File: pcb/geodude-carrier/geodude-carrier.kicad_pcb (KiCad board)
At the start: 2 copper layers, 112.5 x 135.2 mm, 48 parts, among them J1 12V, J2 12V, J3 GND, J30 SCL, J31 SCL, J32 SDA, J33 SDA, J34 3V3, J35 3V3, J36 5V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

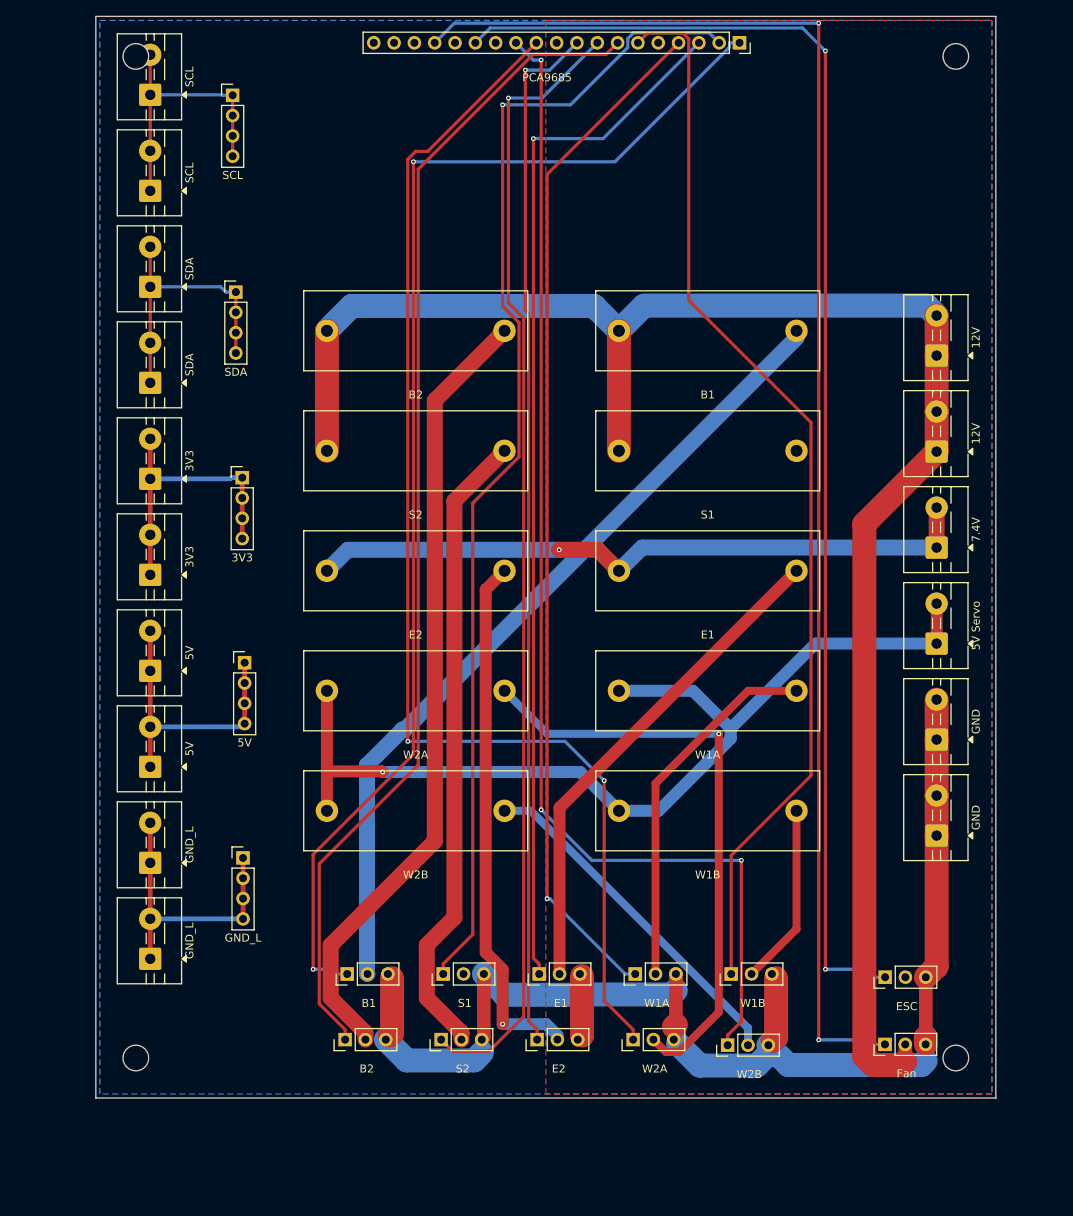
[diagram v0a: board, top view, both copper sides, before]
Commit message: Aligned left terminals and servo rows, unrouted - needs placement review
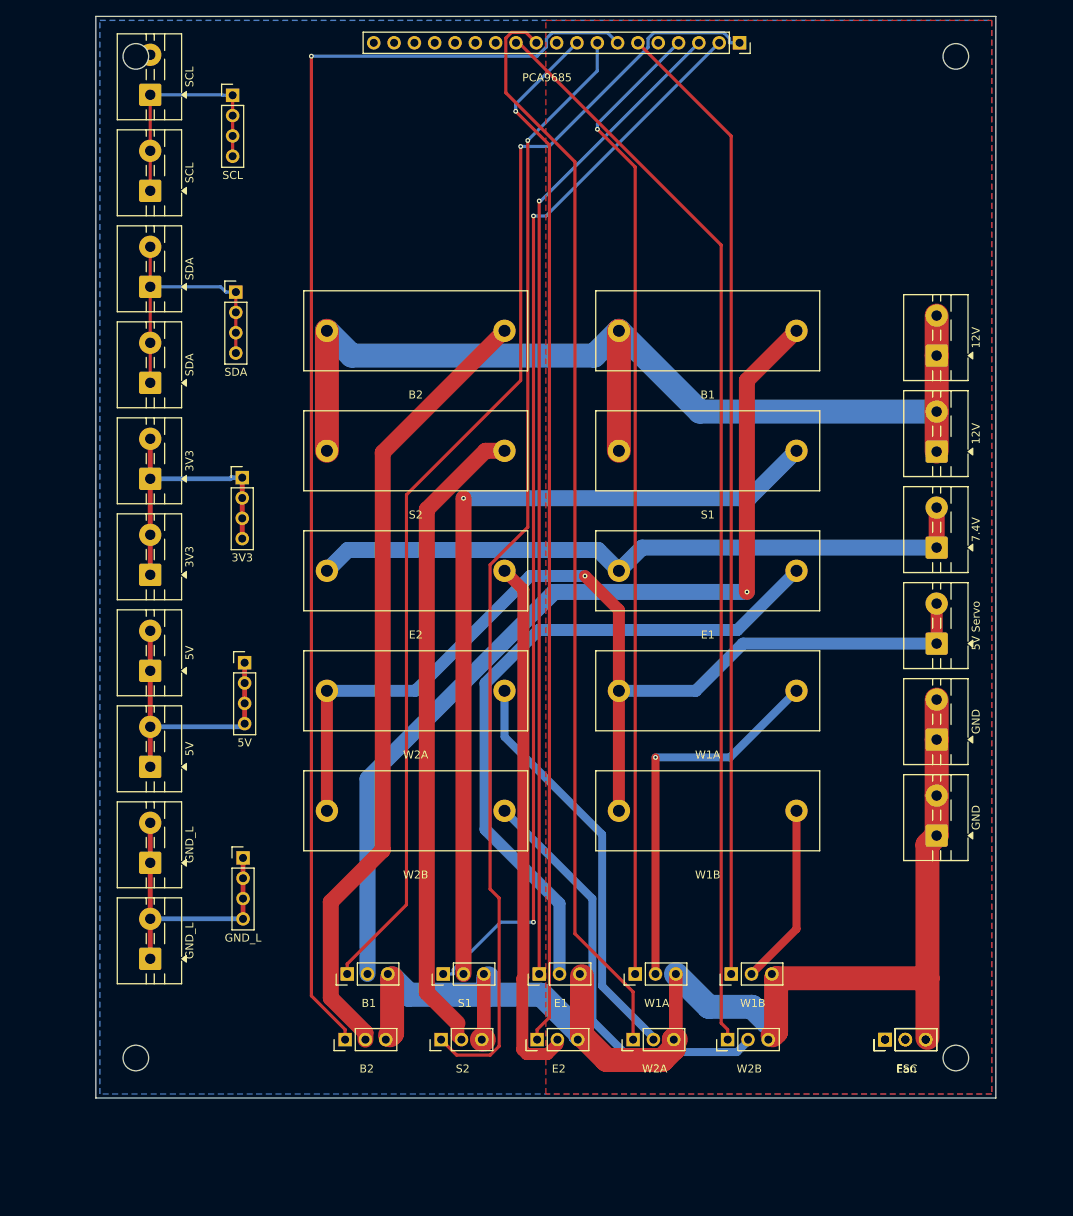
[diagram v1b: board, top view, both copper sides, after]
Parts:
- moved J_ESC 7.80 mm to (116.5, 132.5)
- moved SV10 0.70 mm to (96.8, 132.5)
- moved J_FAN 0.60 mm to (116.4, 132.5)
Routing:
- net PWM_CH12: track 184.6 -> 0.00 mm, vias 2 -> 0
- net PWM_CH11: track 168.4 -> 0.00 mm, vias 2 -> 0
- net SV2_PWR: track 0.00 -> 103.6 mm, vias 0 -> 1
- net +12V: track 214.8 -> 130.0 mm
- net SV9_PWR: track 74.7 -> 51.3 mm, vias 1 -> 0
- net SV3_PWR: track 62.7 -> 84.9 mm
- net PWM_CH8: track 155.3 -> 136.4 mm, vias 2 -> 0
- net PWM_CH5: track 146.7 -> 165.3 mm, vias 0 -> 1
- net SV1_PWR: track 102.8 -> 116.7 mm, vias 0 -> 1
- net PWM_CH9: track 149.2 -> 135.8 mm, vias 3 -> 0
- net PWM_CH4: track 134.6 -> 121.2 mm
- net PWM_CH0: track 157.9 -> 147.2 mm, vias 2 -> 1
- net PWM_CH1: track 145.4 -> 134.7 mm, vias 1 -> 2
- net SV10_PWR: track 43.8 -> 52.6 mm
- net +5V_SERVO: track 123.6 -> 131.5 mm
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
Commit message: Remove duplicate left screw terminals - 1x per bus now
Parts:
- removed J30: SCL, TerminalBlock_MaiXu_MX126-5.0-02P_1x02_P5.00mm
- removed J33: SDA, TerminalBlock_MaiXu_MX126-5.0-02P_1x02_P5.00mm
- removed J35: 3V3, TerminalBlock_MaiXu_MX126-5.0-02P_1x02_P5.00mm
- removed J36: 5V, TerminalBlock_MaiXu_MX126-5.0-02P_1x02_P5.00mm
- removed J38: GND_L, TerminalBlock_MaiXu_MX126-5.0-02P_1x02_P5.00mm

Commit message: Left bus: screw+header pairs aligned, 12mm spacing
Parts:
- moved J44 35.3 mm to (24.0, 76.7)
- moved J39 34.8 mm to (12.0, 78.0)
- moved J43 24.1 mm to (24.0, 64.7)
- moved J37 24.0 mm to (12.0, 66.0)
- moved J31 20.1 mm to (12.0, 30.0)
- moved J40 17.9 mm to (24.0, 28.7)
- moved J42 15.4 mm to (24.0, 52.7)
- moved J34 15.1 mm to (12.0, 54.0)
- moved J32 13.1 mm to (12.0, 42.0)
- moved J41 11.4 mm to (24.0, 40.7)
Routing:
- net GND_LOGIC: track 36.2 -> 53.2 mm
- net +5V_LOGIC: track 36.6 -> 19.6 mm
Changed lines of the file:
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@@
 	(footprint "PinHeader_1x04_P2.54mm_Vertical"
 		(layer "F.Cu")
-		(at 35.3 39.06)
+		(at 24 40.7)
 		(descr "Through hole straight pin header, 1x04, 2.54mm pitch, single row")
 		(tags "Through hole pin header THT 1x04 2.54mm single row")
@@
 	(footprint "TerminalBlock_MaiXu_MX126-5.0-02P_1x02_P5.00mm"
 		(layer "F.Cu")
-		(at 24.6 62.4 90)
+		(at 12 54 90)
 		(descr "terminal block MaiXu MX126-5.0-02P, 2 pins, pitch 5mm, size 10.5x7.8mm, drill diameter 1.3mm, pad diameter 2.8mm, https://www.lcsc.com/datasheet/lcsc_datasheet_2309150913_MAX-MX126-5-0-03P-GN01-Cu-S-A_C5188435.pdf")
 		(tags "THT terminal block MaiXu MX126-5.0-02P pitch 5mm size 10.5x7.8mm drill 1.3mm pad 2.8mm")
@@
 	(footprint "TerminalBlock_MaiXu_MX126-5.0-02P_1x02_P5.00mm"
 		(layer "F.Cu")
-		(at 24.6 38.4 90)
+		(at 12 42 90)
 		(descr "terminal block MaiXu MX126-5.0-02P, 2 pins, pitch 5mm, size 10.5x7.8mm, drill diameter 1.3mm, pad diameter 2.8mm, https://www.lcsc.com/datasheet/lcsc_datasheet_2309150913_MAX-MX126-5-0-03P-GN01-Cu-S-A_C5188435.pdf")
 		(tags "THT terminal block MaiXu MX126-5.0-02P pitch 5mm size 10.5x7.8mm drill 1.3mm pad 2.8mm")
@@
 	(footprint "TerminalBlock_MaiXu_MX126-5.0-02P_1x02_P5.00mm"
 		(layer "F.Cu")
-		(at 24.6 86.4 90)
+		(at 12 66 90)
 		(descr "terminal block MaiXu MX126-5.0-02P, 2 pins, pitch 5mm, size 10.5x7.8mm, drill diameter 1.3mm, pad diameter 2.8mm, https://www.lcsc.com/datasheet/lcsc_datasheet_2309150913_MAX-MX126-5-0-03P-GN01-Cu-S-A_C5188435.pdf")
 		(tags "THT terminal block MaiXu MX126-5.0-02P pitch 5mm size 10.5x7.8mm drill 1.3mm pad 2.8mm")
@@
 	(footprint "PinHeader_1x04_P2.54mm_Vertical"
 		(layer "F.Cu")
-		(at 36.2 109.79)
+		(at 24 76.7)
 		(descr "Through hole straight pin header, 1x04, 2.54mm pitch, single row")
 		(tags "Through hole pin header THT 1x04 2.54mm single row")
@@
 	(footprint "PinHeader_1x04_P2.54mm_Vertical"
 		(layer "F.Cu")
-		(at 36.4 85.39)
+		(at 24 64.7)
 		(descr "Through hole straight pin header, 1x04, 2.54mm pitch, single row")
 		(tags "Through hole pin header THT 1x04 2.54mm single row")
@@
 	(footprint "TerminalBlock_MaiXu_MX126-5.0-02P_1x02_P5.00mm"
 		(layer "F.Cu")
-		(at 24.6 110.4 90)
+		(at 12 78 90)
 		(descr "terminal block MaiXu MX126-5.0-02P, 2 pins, pitch 5mm, size 10.5x7.8mm, drill diameter 1.3mm, pad diameter 2.8mm, https://www.lcsc.com/datasheet/lcsc_datasheet_2309150913_MAX-MX126-5-0-03P-GN01-Cu-S-A_C5188435.pdf")
 		(tags "THT terminal block MaiXu MX126-5.0-02P pitch 5mm size 10.5x7.8mm drill 1.3mm pad 2.8mm")
@@
 	(footprint "PinHeader_1x04_P2.54mm_Vertical"
 		(layer "F.Cu")
-		(at 34.9 14.46)
+		(at 24 28.7)
 		(descr "Through hole straight pin header, 1x04, 2.54mm pitch, single row")
 		(tags "Through hole pin header THT 1x04 2.54mm single row")
@@
 	(footprint "TerminalBlock_MaiXu_MX126-5.0-02P_1x02_P5.00mm"
 		(layer "F.Cu")
-		(at 24.6 14.4 90)
+		(at 12 30 90)
 		(descr "terminal block MaiXu MX126-5.0-02P, 2 pins, pitch 5mm, size 10.5x7.8mm, drill diameter 1.3mm, pad diameter 2.8mm, https://www.lcsc.com/datasheet/lcsc_datasheet_2309150913_MAX-MX126-5-0-03P-GN01-Cu-S-A_C5188435.pdf")
 		(tags "THT terminal block MaiXu MX126-5.0-02P pitch 5mm size 10.5x7.8mm drill 1.3mm pad 2.8mm")
@@
 	(footprint "PinHeader_1x04_P2.54mm_Vertical"
 		(layer "F.Cu")
-		(at 36.1 62.26)
+		(at 24 52.7)
 		(descr "Through hole straight pin header, 1x04, 2.54mm pitch, single row")
 		(tags "Through hole pin header THT 1x04 2.54mm single row")
@@
 	)
 	(segment
-		(start 24.6 93.4)
-		(end 24.6 86.4)
-		(width 0.6)
-		(layer "F.Cu")
-		(net "+5V_LOGIC")
-	)
-	(segment
-		(start 24.6 81.4)
-		(end 24.6 86.4)
-		(width 0.6)
-		(layer "F.Cu")
-		(net "+5V_LOGIC")
-	)
-	(segment
-		(start 24.6 98.4)
-		(end 24.6 93.4)
-		(width 0.6)
-		(layer "F.Cu")
-		(net "+5V_LOGIC")
-	)
-	(segment
 		(start 36.4 93.01)
 		(end 36.4 90.47)
@@
 	)
 	(segment
+		(start 24.6 93.4)
+		(end 24.6 86.4)
+		(width 0.6)
+		(layer "F.Cu")
+		(net "GND_LOGIC")
+	)
+	(segment
 		(start 24.6 117.4)
 		(end 24.6 110.4)
@@
 		(width 0.6)
 		(layer "F.Cu")
+		(net "GND_LOGIC")
+	)
+	(segment
+		(start 24.6 81.4)
+		(end 24.6 86.4)
+		(width 0.6)
+		(layer "F.Cu")
+		(net "GND_LOGIC")
+	)
+	(segment
+		(start 24.6 98.4)
+		(end 24.6 93.4)
+		(width 0.6)
+		(layer "F.Cu")

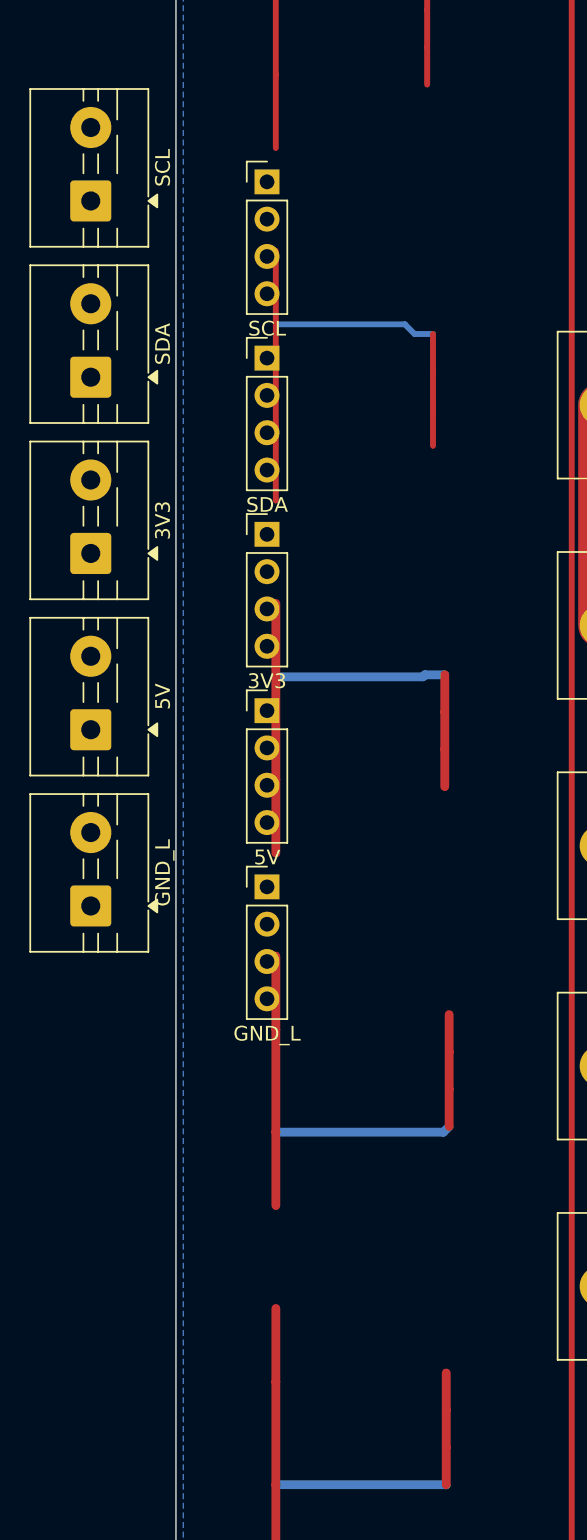
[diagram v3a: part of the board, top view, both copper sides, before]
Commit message: Spacing update
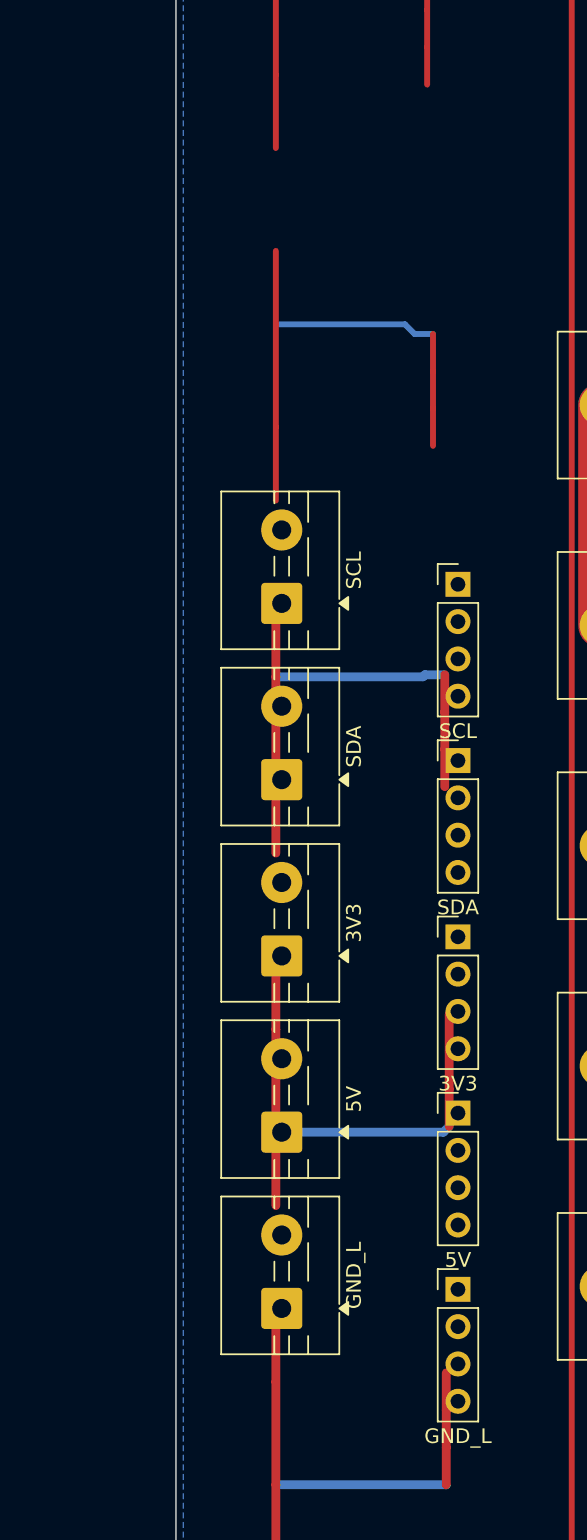
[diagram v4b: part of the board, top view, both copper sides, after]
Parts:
- moved J40 30.3 mm to (37.0, 56.1)
- moved J31 30.3 mm to (25.0, 57.4)
- moved J32 30.3 mm to (25.0, 69.4)
- moved J34 30.3 mm to (25.0, 81.4)
- moved J37 30.3 mm to (25.0, 93.4)
- moved J39 30.3 mm to (25.0, 105.4)
- moved J41 30.3 mm to (37.0, 68.1)
- moved J42 30.3 mm to (37.0, 80.1)
- moved J43 30.3 mm to (37.0, 92.1)
- moved J44 30.3 mm to (37.0, 104.1)
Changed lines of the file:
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@@
 	(footprint "PinHeader_1x04_P2.54mm_Vertical"
 		(layer "F.Cu")
-		(at 24 40.7)
+		(at 37 68.1)
 		(descr "Through hole straight pin header, 1x04, 2.54mm pitch, single row")
 		(tags "Through hole pin header THT 1x04 2.54mm single row")
@@
 	(footprint "TerminalBlock_MaiXu_MX126-5.0-02P_1x02_P5.00mm"
 		(layer "F.Cu")
-		(at 12 54 90)
+		(at 25 81.4 90)
 		(descr "terminal block MaiXu MX126-5.0-02P, 2 pins, pitch 5mm, size 10.5x7.8mm, drill diameter 1.3mm, pad diameter 2.8mm, https://www.lcsc.com/datasheet/lcsc_datasheet_2309150913_MAX-MX126-5-0-03P-GN01-Cu-S-A_C5188435.pdf")
 		(tags "THT terminal block MaiXu MX126-5.0-02P pitch 5mm size 10.5x7.8mm drill 1.3mm pad 2.8mm")
@@
 	(footprint "TerminalBlock_MaiXu_MX126-5.0-02P_1x02_P5.00mm"
 		(layer "F.Cu")
-		(at 12 42 90)
+		(at 25 69.4 90)
 		(descr "terminal block MaiXu MX126-5.0-02P, 2 pins, pitch 5mm, size 10.5x7.8mm, drill diameter 1.3mm, pad diameter 2.8mm, https://www.lcsc.com/datasheet/lcsc_datasheet_2309150913_MAX-MX126-5-0-03P-GN01-Cu-S-A_C5188435.pdf")
 		(tags "THT terminal block MaiXu MX126-5.0-02P pitch 5mm size 10.5x7.8mm drill 1.3mm pad 2.8mm")
@@
 	(footprint "TerminalBlock_MaiXu_MX126-5.0-02P_1x02_P5.00mm"
 		(layer "F.Cu")
-		(at 12 66 90)
+		(at 25 93.4 90)
 		(descr "terminal block MaiXu MX126-5.0-02P, 2 pins, pitch 5mm, size 10.5x7.8mm, drill diameter 1.3mm, pad diameter 2.8mm, https://www.lcsc.com/datasheet/lcsc_datasheet_2309150913_MAX-MX126-5-0-03P-GN01-Cu-S-A_C5188435.pdf")
 		(tags "THT terminal block MaiXu MX126-5.0-02P pitch 5mm size 10.5x7.8mm drill 1.3mm pad 2.8mm")
@@
 	(footprint "PinHeader_1x04_P2.54mm_Vertical"
 		(layer "F.Cu")
-		(at 24 76.7)
+		(at 37 104.1)
 		(descr "Through hole straight pin header, 1x04, 2.54mm pitch, single row")
 		(tags "Through hole pin header THT 1x04 2.54mm single row")
@@
 	(footprint "PinHeader_1x04_P2.54mm_Vertical"
 		(layer "F.Cu")
-		(at 24 64.7)
+		(at 37 92.1)
 		(descr "Through hole straight pin header, 1x04, 2.54mm pitch, single row")
 		(tags "Through hole pin header THT 1x04 2.54mm single row")
@@
 	(footprint "TerminalBlock_MaiXu_MX126-5.0-02P_1x02_P5.00mm"
 		(layer "F.Cu")
-		(at 12 78 90)
+		(at 25 105.4 90)
 		(descr "terminal block MaiXu MX126-5.0-02P, 2 pins, pitch 5mm, size 10.5x7.8mm, drill diameter 1.3mm, pad diameter 2.8mm, https://www.lcsc.com/datasheet/lcsc_datasheet_2309150913_MAX-MX126-5-0-03P-GN01-Cu-S-A_C5188435.pdf")
 		(tags "THT terminal block MaiXu MX126-5.0-02P pitch 5mm size 10.5x7.8mm drill 1.3mm pad 2.8mm")
@@
 	(footprint "PinHeader_1x04_P2.54mm_Vertical"
 		(layer "F.Cu")
-		(at 24 28.7)
+		(at 37 56.1)
 		(descr "Through hole straight pin header, 1x04, 2.54mm pitch, single row")
 		(tags "Through hole pin header THT 1x04 2.54mm single row")
@@
 	(footprint "TerminalBlock_MaiXu_MX126-5.0-02P_1x02_P5.00mm"
 		(layer "F.Cu")
-		(at 12 30 90)
+		(at 25 57.4 90)
 		(descr "terminal block MaiXu MX126-5.0-02P, 2 pins, pitch 5mm, size 10.5x7.8mm, drill diameter 1.3mm, pad diameter 2.8mm, https://www.lcsc.com/datasheet/lcsc_datasheet_2309150913_MAX-MX126-5-0-03P-GN01-Cu-S-A_C5188435.pdf")
 		(tags "THT terminal block MaiXu MX126-5.0-02P pitch 5mm size 10.5x7.8mm drill 1.3mm pad 2.8mm")
@@
 	(footprint "PinHeader_1x04_P2.54mm_Vertical"
 		(layer "F.Cu")
-		(at 24 52.7)
+		(at 37 80.1)
 		(descr "Through hole straight pin header, 1x04, 2.54mm pitch, single row")
 		(tags "Through hole pin header THT 1x04 2.54mm single row")
